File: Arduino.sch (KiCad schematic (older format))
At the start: 1 part

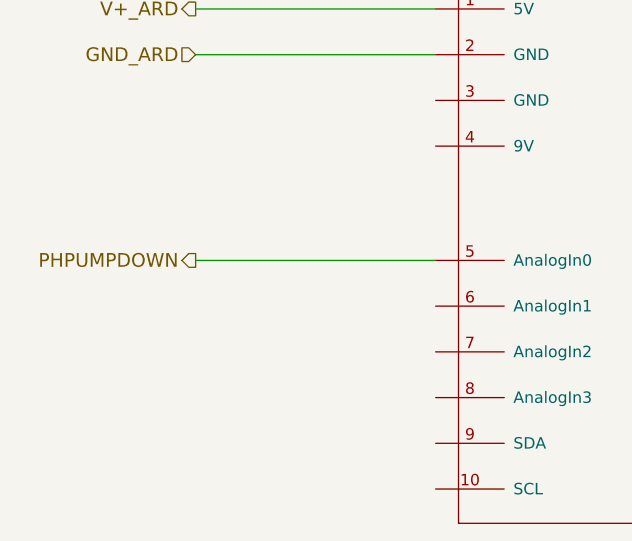
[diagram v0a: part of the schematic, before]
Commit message: added 2nd pump in circuit to accomodate pH UP
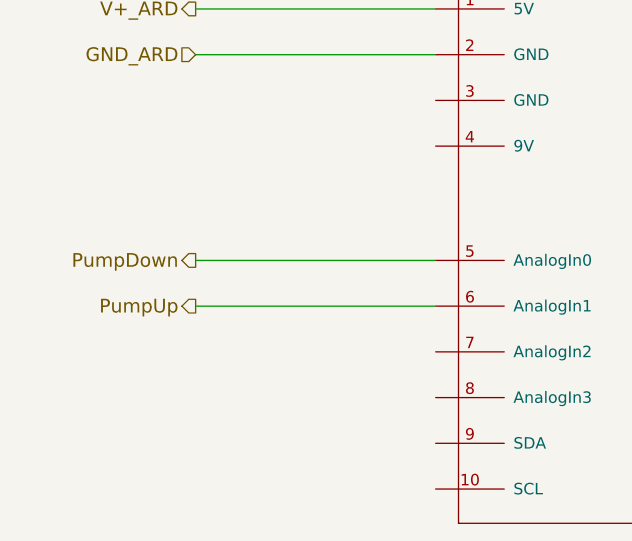
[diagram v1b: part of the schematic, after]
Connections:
- net PumpUp: now reaches ARD1.6 (AnalogIn1)
- net PHPUMPDOWN renamed PumpDown
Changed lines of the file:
@@
 $Descr A4 11693 8268
 encoding utf-8
-Sheet 6 7
+Sheet 5 7
 Title ""
-Date "11 aug 2014"
+Date "12 aug 2014"
 Rev ""
 Comp ""
@@
 	5750 2600 6350 2600
 Text HLabel 2500 3550 0    60   Output ~ 0
-PHPUMPDOWN
+PumpDown
 Text HLabel 6400 3800 2    60   Output ~ 0
 ~RESET
@@
 Wire Wire Line
 	3550 3550 2500 3550
+Text HLabel 2500 3750 0    60   Output ~ 0
+PumpUp
+Wire Wire Line
+	2500 3750 3550 3750
 $EndSCHEMATC
